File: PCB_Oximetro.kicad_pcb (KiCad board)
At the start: 2 copper layers, 79.5 x 57.9 mm, 20 parts, among them J1 USB_A, J2 Conn_01x08, SW1 SW_Push, U1 LM1117MP-1.8, U2 MAX30102, U3 LM1117MP-3.3, U5 ESP32-DEVKIT-V1

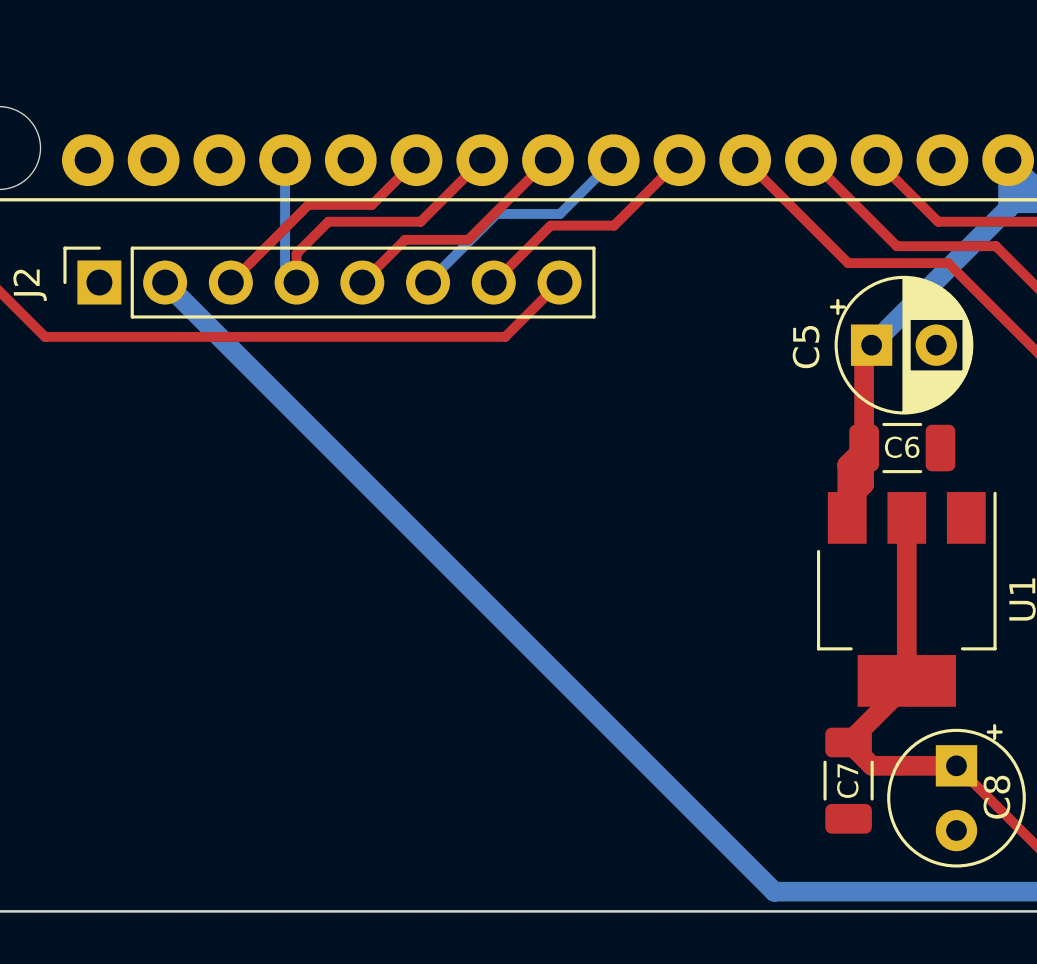
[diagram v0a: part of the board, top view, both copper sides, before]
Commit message: I2C Adjust
Added I2C and INT pull up resistor
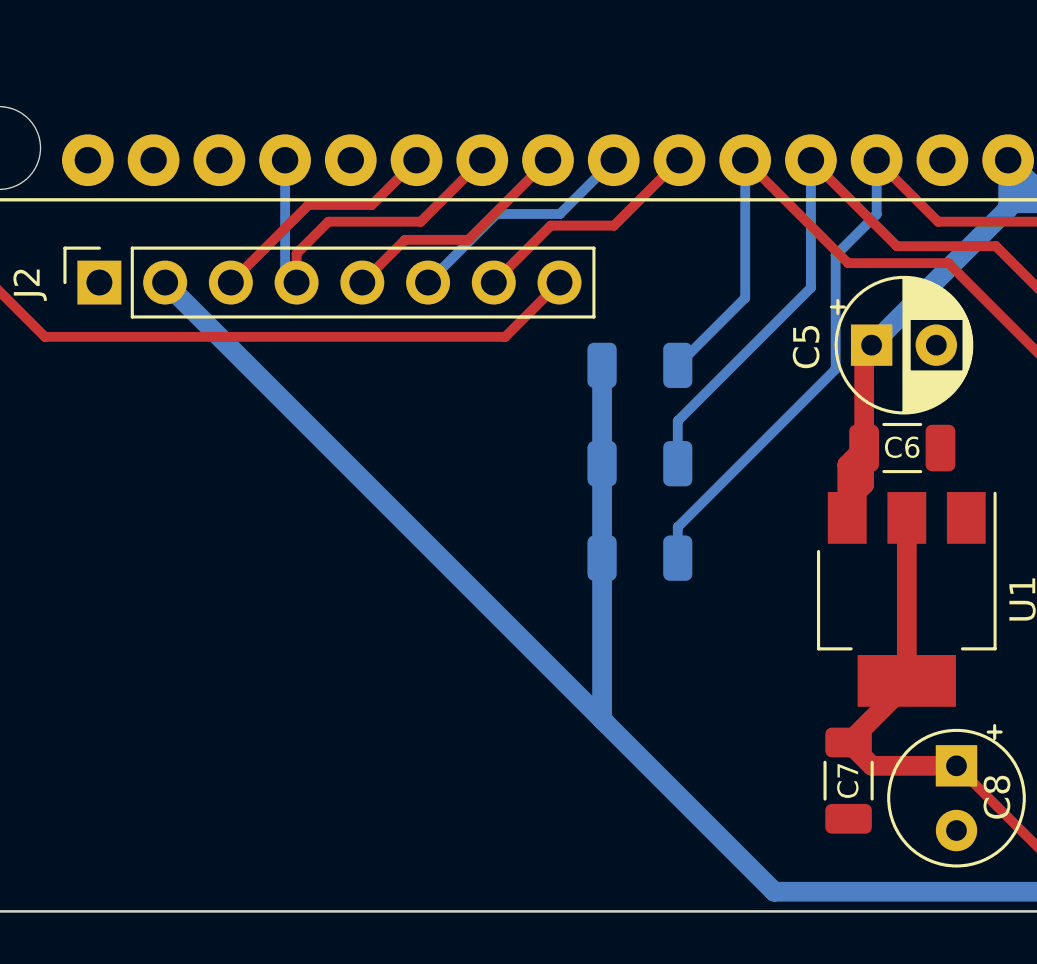
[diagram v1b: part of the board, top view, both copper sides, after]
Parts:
- added R3: 4K7, Resistor_SMD:R_1206_3216Metric, B.Cu at (123.8, 98.3)
- added R4: 4K7, Resistor_SMD:R_1206_3216Metric, B.Cu at (123.8, 94.5)
- added R5: 4K7, Resistor_SMD:R_1206_3216Metric, B.Cu at (123.8, 102.0)
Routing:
- net INT: track 32.5 -> 51.0 mm
- net 3V3: track 90.1 -> 104.0 mm
- net SCL: track 32.4 -> 46.2 mm
- net SDA: track 33.7 -> 42.7 mm

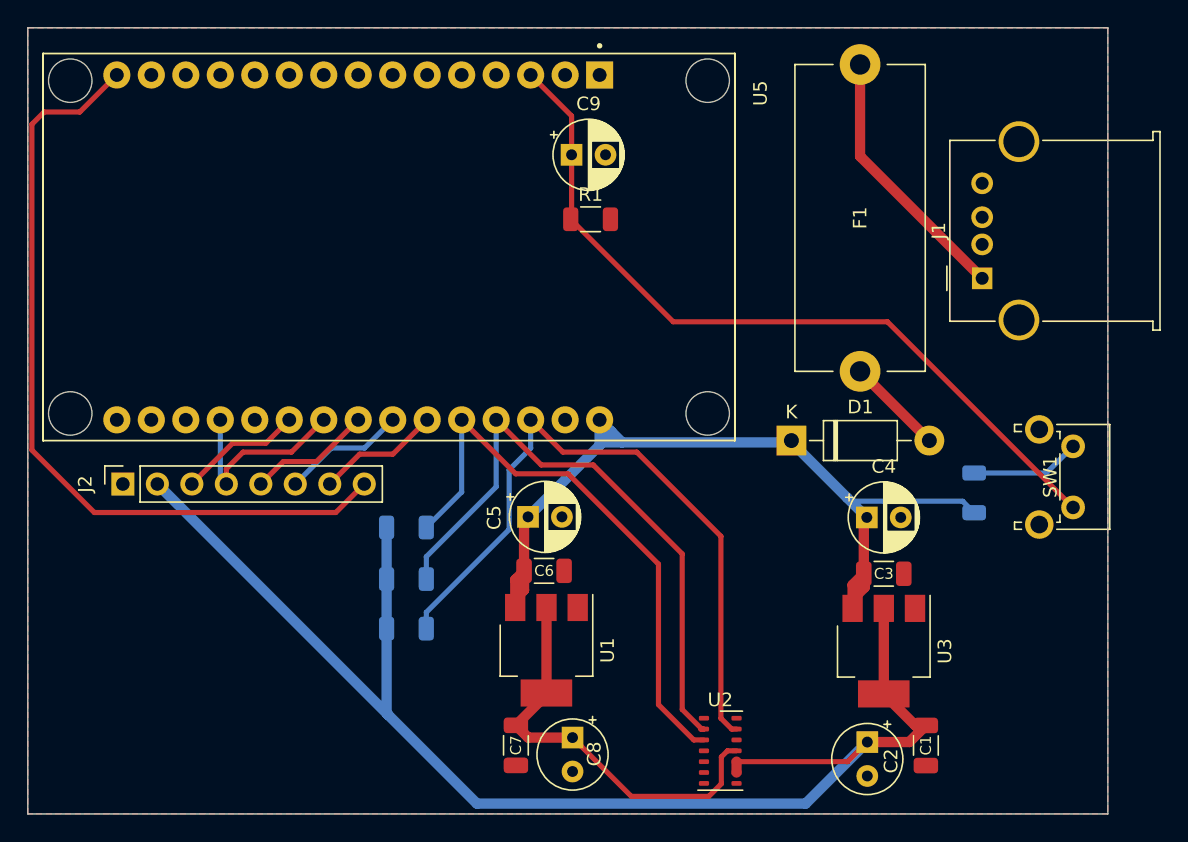
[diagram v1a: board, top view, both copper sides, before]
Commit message: Oximeter change
Removed MAX30102 sensor and added MAX30102 shield
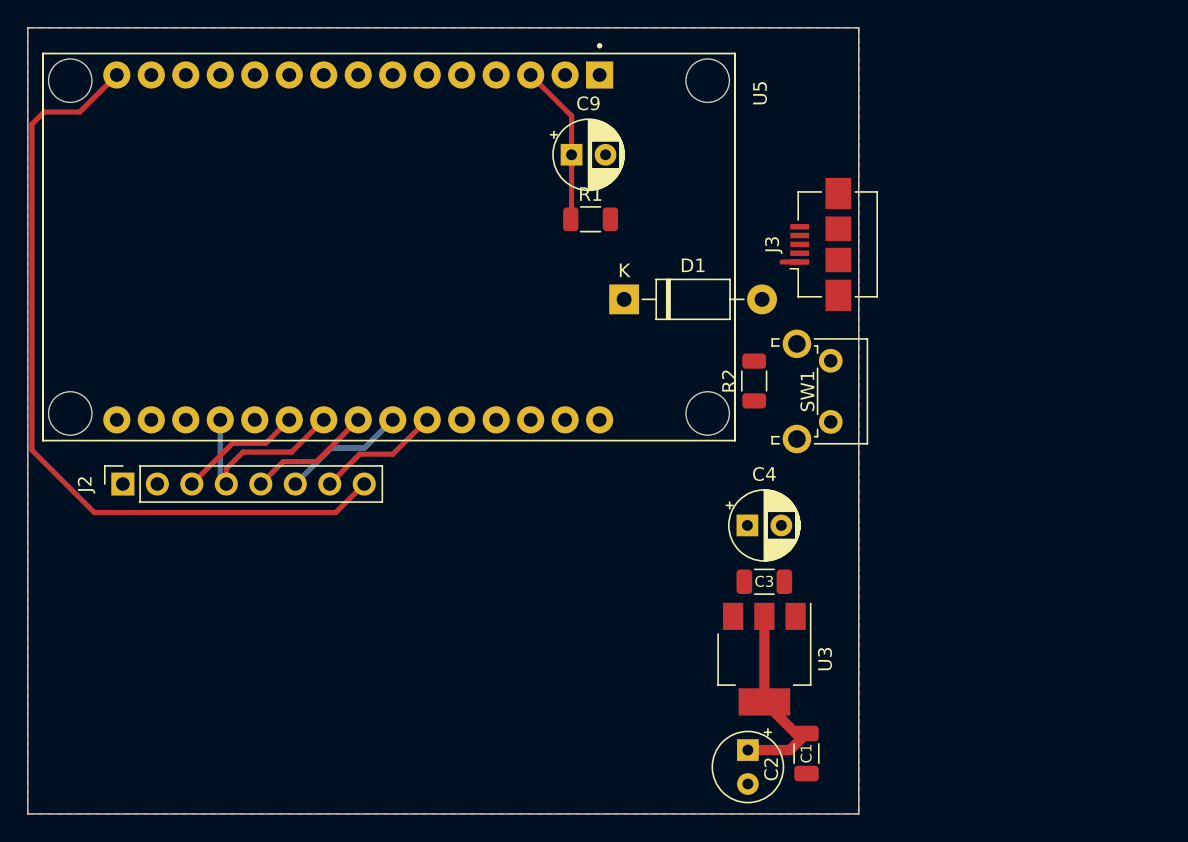
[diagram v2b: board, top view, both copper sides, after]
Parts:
- removed C5: 10uF, Capacitor_THT:CP_Radial_D5.0mm_P2.50mm
- removed C6, C7: 100nF, Capacitor_SMD:C_1206_3216Metric
- removed C8: 22uF, Capacitor_THT:CP_Radial_Tantal_D5.0mm_P2.50mm
- removed F1: 500mA, Fuse:Fuseholder_Cylinder-5x20mm_Stelvio-Kontek_PTF78_Horizontal_Open
- removed J1: USB_A, Connector_USB:USB_A_Molex_67643_Horizontal
- removed R3, R4, R5: 4K7, Resistor_SMD:R_1206_3216Metric
- removed U1: LM1117MP-1.8, Package_TO_SOT_SMD:SOT-223-3_TabPin2
- removed U2: MAX30102, OptoDevice:Maxim_OLGA-14_3.3x5.6mm_P0.8mm
- added J3: USB_B_Micro, Connector_USB:USB_Micro-B_Amphenol_10104110_Horizontal, F.Cu at (154.3, 73.7)
- R2: moved to F.Cu
- moved SW1 18.9 mm to (155.0, 82.2)
- moved R2 18.2 mm to (149.4, 83.7)
- moved D1 16.1 mm to (139.8, 77.7)
- moved C1 8.81 mm to (153.2, 111.2)
- moved C3 8.81 mm to (150.2, 98.5)
- moved U3 8.81 mm to (150.2, 104.2)
- moved C2 8.81 mm to (148.9, 110.9)
- moved C4 8.81 mm to (148.9, 94.3)
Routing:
- net 3V3: track 104.0 -> 15.2 mm
- net +5V: track 63.2 -> 0.00 mm
- net INT: track 51.0 -> 0.00 mm
- net BTT: track 57.7 -> 11.9 mm
- net SCL: track 46.2 -> 0.68 mm
- net SDA: track 42.7 -> 0.00 mm
- net 1V8: track 30.6 -> 0.00 mm
- net Net-(J1-VBUS): track 19.5 -> 0.00 mm
- net Net-(R2-Pad2): track 8.10 -> 0.00 mm
- net Net-(D1-A): track 7.21 -> 1.30 mm
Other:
- board size 79.5 x 57.9 mm -> 61.2 x 57.9 mm

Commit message: PCB Layout
Changed pcb layout for MAX30102 module
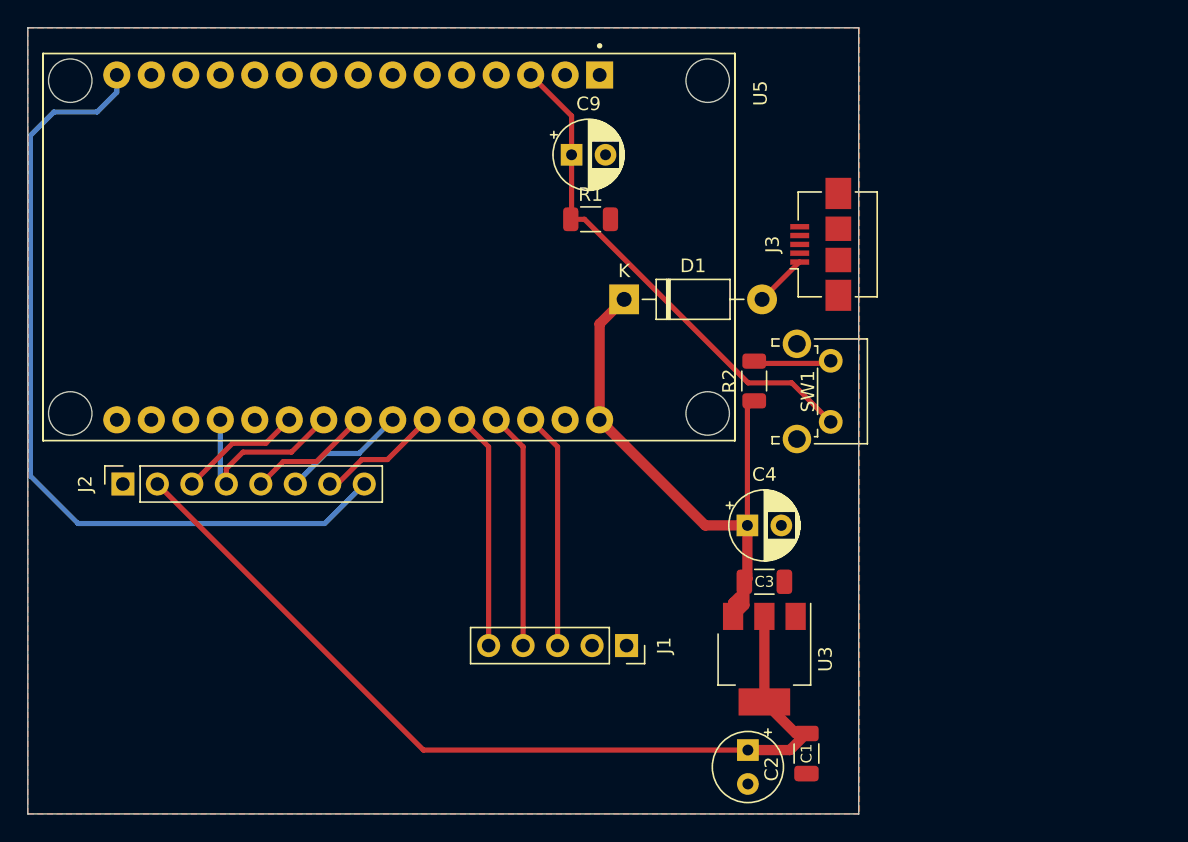
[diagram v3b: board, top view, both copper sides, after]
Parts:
- added J1: Conn_01x05, Connector_PinSocket_2.54mm:PinSocket_1x05_P2.54mm_Vertical, F.Cu at (140.0, 103.2)
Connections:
- U5 pad 26: SDA -> INT
- U5 pad 27: SCL -> SDA
- U5 pad 28: INT -> SCL
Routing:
- net 3V3: track 15.2 -> 66.8 mm
- net +5V: track 0.00 -> 41.9 mm
- net BTT: track 11.9 -> 37.2 mm
- net SDA: track 0.00 -> 18.1 mm
- net INT: track 0.00 -> 17.4 mm
- net SCL: track 0.68 -> 17.4 mm
- net Net-(R2-Pad2): track 0.00 -> 5.78 mm
- net Net-(D1-A): track 1.30 -> 3.91 mm
- net BLK: track 59.0 -> 61.3 mm
